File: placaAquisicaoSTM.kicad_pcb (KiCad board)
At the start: 2 copper layers, 55 parts, among them IC1 STM32H523CET6, J1 Conn_01x05, J2 Conn_02x06_Counter_Clockwise, SW1 SW_Push, SW2 SW_SPDT, U1 AMS1117-3.3, U10 PC817, U11 AMS1117-5.0, U12 SN65HVD230, U2 PC817, U3 PC817, U4 PC817, U5 PC817, U6 PC817, U7 PC817, U8 PC817

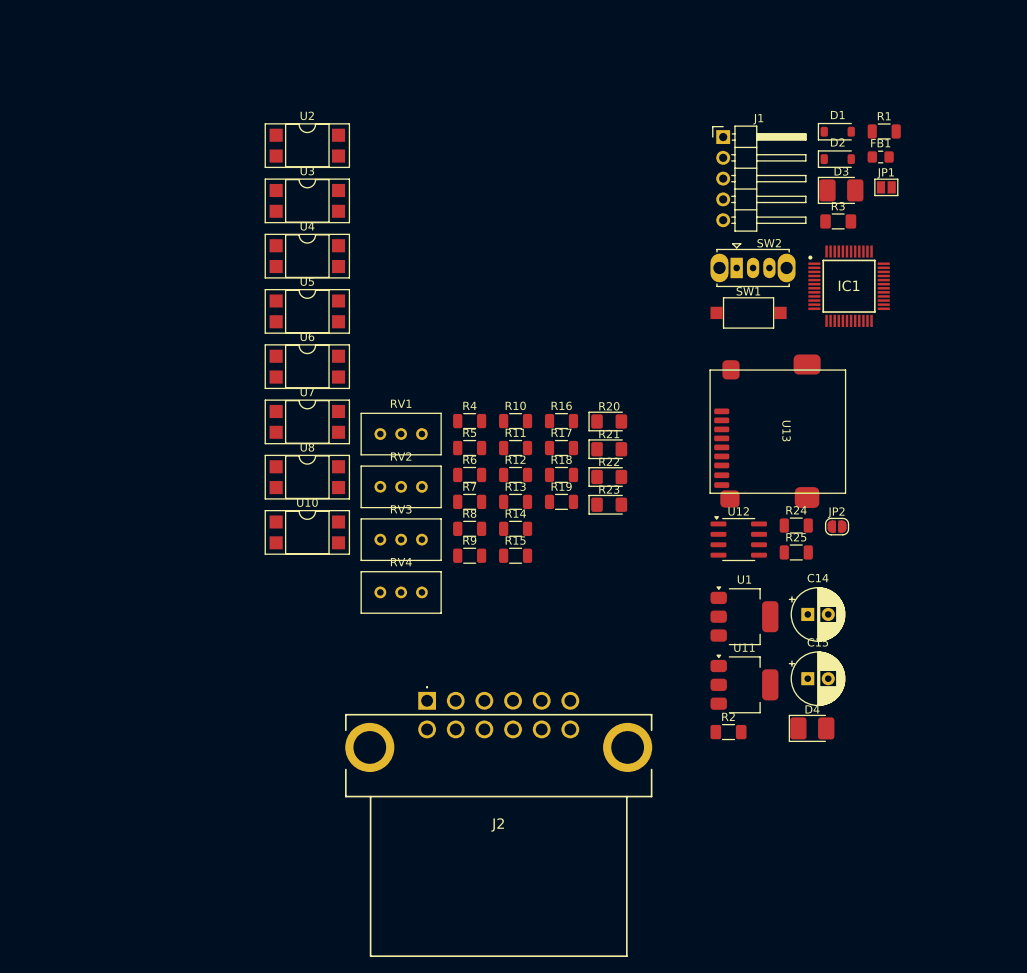
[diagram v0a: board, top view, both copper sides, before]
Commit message: Removi as entradas analógicas, projeto delas estava errado
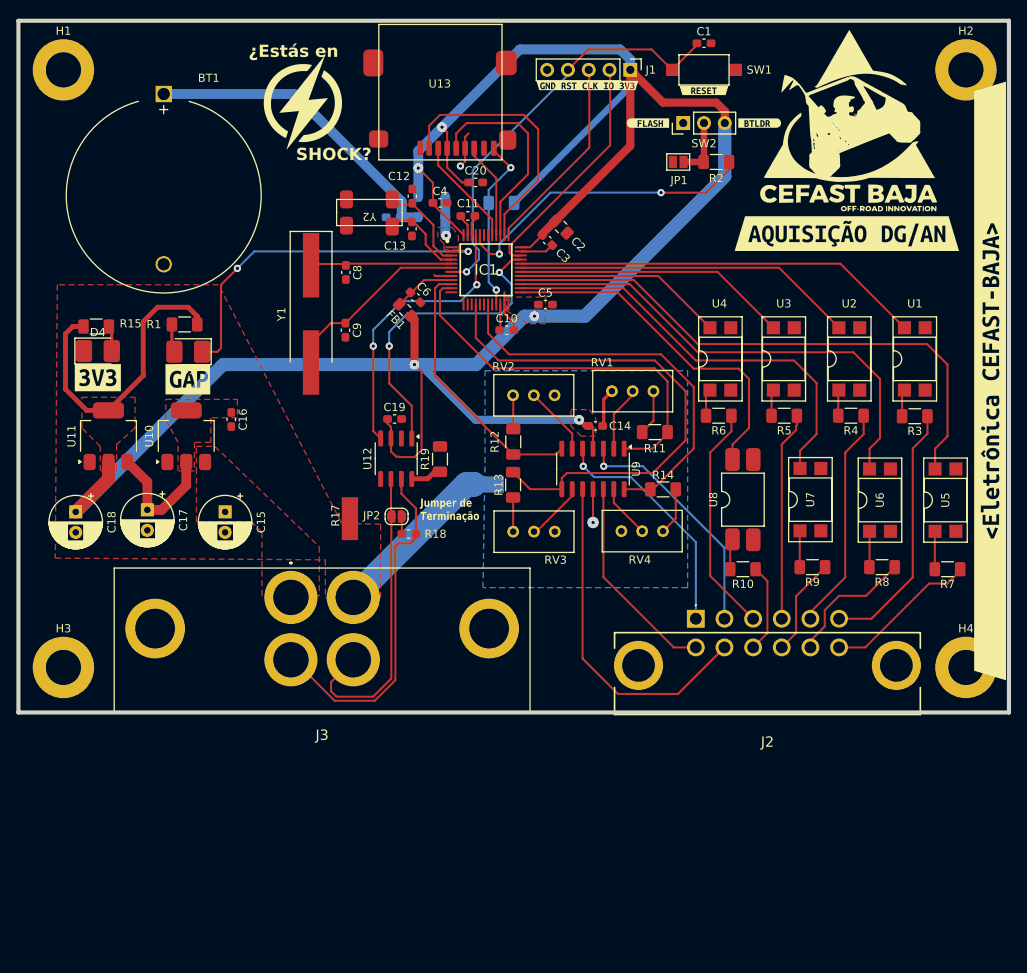
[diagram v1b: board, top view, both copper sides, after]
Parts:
- removed the R10 at (124.2, 93.9)
- removed the R11 at (124.2, 97.2)
- removed the R14 at (124.2, 107.1)
- removed the R19 at (129.8, 103.8)
- removed R25: 120, Resistor_SMD:R_1206_3216Metric
- removed the R6 at (118.6, 100.5)
- removed the R7 at (118.6, 103.8)
- added BT1: Battery_Cell, Battery:BatteryHolder_MYOUNG_BS-07-A1BJ001_CR2032, F.Cu at (81.2, 54.0)
- added C1: 100n, Capacitor_SMD:C_0603_1608Metric_Pad1.08x0.95mm_HandSolder, F.Cu at (147.2, 47.8)
- added C10: 2u2, Capacitor_SMD:C_0603_1608Metric_Pad1.08x0.95mm_HandSolder, F.Cu at (123.2, 82.8)
- added C11: 2u2, Capacitor_SMD:C_0603_1608Metric_Pad1.08x0.95mm_HandSolder, F.Cu at (118.4, 68.8)
- added C12: 22p, Capacitor_SMD:C_0603_1608Metric_Pad1.08x0.95mm_HandSolder, F.Cu at (111.6, 66.4)
- added C13: 22p, Capacitor_SMD:C_0603_1608Metric_Pad1.08x0.95mm_HandSolder, F.Cu at (111.6, 70.4)
- added C14: 1n, Capacitor_SMD:C_0603_1608Metric_Pad1.08x0.95mm_HandSolder, F.Cu at (134.0, 94.5)
- added C15: 22u, Capacitor_THT:CP_Radial_D6.3mm_P2.50mm, F.Cu at (88.8, 105.0)
- added C16: 100n, Capacitor_SMD:C_0603_1608Metric_Pad1.08x0.95mm_HandSolder, F.Cu at (89.5, 93.7)
- added C19: 1n, Capacitor_SMD:C_0603_1608Metric_Pad1.08x0.95mm_HandSolder, F.Cu at (109.5, 93.7)
- added C2: 4u7, Capacitor_SMD:C_0805_2012Metric_Pad1.18x1.45mm_HandSolder, F.Cu at (129.8, 70.2)
- added C20: 1n, Capacitor_SMD:C_0603_1608Metric_Pad1.08x0.95mm_HandSolder, F.Cu at (119.3, 64.8)
- added C3: 100n, Capacitor_SMD:C_0603_1608Metric_Pad1.08x0.95mm_HandSolder, F.Cu at (128.1, 71.8)
- added C4: 100n, Capacitor_SMD:C_0603_1608Metric_Pad1.08x0.95mm_HandSolder, F.Cu at (115.0, 67.2)
- added C5: 100n, Capacitor_SMD:C_0603_1608Metric_Pad1.08x0.95mm_HandSolder, F.Cu at (127.9, 79.7)
- added C6: 10n, Capacitor_SMD:C_0603_1608Metric_Pad1.08x0.95mm_HandSolder, F.Cu at (112.0, 78.8)
- added C7: 100n, Capacitor_SMD:C_0603_1608Metric_Pad1.08x0.95mm_HandSolder, B.Cu at (109.3, 69.0)
- added C8: 22p, Capacitor_SMD:C_0603_1608Metric_Pad1.08x0.95mm_HandSolder, F.Cu at (103.5, 75.8)
- added C9: 22p, Capacitor_SMD:C_0603_1608Metric_Pad1.08x0.95mm_HandSolder, F.Cu at (103.5, 82.8)
- added G***: LOGO, Baja_Library:Raio_Circulo, F.Cu at (98.2, 55.0)
- added G***: LOGO, Baja_Library:LogoBaja, F.Cu at (164.9, 57.2)
- added G***: LOGO, Baja_Library:communism, B.Cu at (172.2, 105.0)
- added G***: LOGO, Baja_Library:Raio_Circulo, B.Cu at (160.3, 102.8)
- added G***: LOGO, Baja_Library:LogoBaja, B.Cu at (165.0, 57.4)
- added H1: MountingHole, MountingHole:MountingHole_4.3mm_M4_DIN965_Pad, F.Cu at (69.0, 51.0)
- added H2: MountingHole, MountingHole:MountingHole_4.3mm_M4_DIN965_Pad, F.Cu at (179.2, 51.0)
- added H3: MountingHole, MountingHole:MountingHole_4.3mm_M4_DIN965_Pad, F.Cu at (69.0, 124.0)
- added H4: MountingHole, MountingHole:MountingHole_4.3mm_M4_DIN965_Pad, F.Cu at (179.2, 124.0)
- added J3: Conn_02x02_Top_Bottom, Baja_Library:MX150L_4P, F.Cu at (96.8, 115.4)
- added R18: 120, Capacitor_SMD:C_0603_1608Metric_Pad1.08x0.95mm_HandSolder, F.Cu at (111.2, 107.7)
- added R20: 10k, Resistor_SMD:R_1206_3216Metric_Pad1.30x1.75mm_HandSolder, B.Cu at (122.5, 67.2)
- added U9: LM324, Package_SO:SOIC-14_3.9x8.7mm_P1.27mm, F.Cu at (133.7, 99.8)
- added Y1: Crystal, Crystal:Crystal_SMD_HC49-SD_HandSoldering, F.Cu at (99.2, 80.8)
- added Y2: Crystal_GND23, Baja_Library:DMX-26S, F.Cu at (106.4, 68.4)
- added kibuzzard-67572A93: G***, kibuzzard-67572A93, F.Cu at (140.4, 57.5)
- added kibuzzard-67572AD3: G***, kibuzzard-67572AD3, F.Cu at (154.1, 57.5)
- added kibuzzard-67572B0D: G***, kibuzzard-67572B0D, F.Cu at (147.2, 53.5)
- added kibuzzard-6758F1AD: G***, kibuzzard-6758F1AD, F.Cu at (84.2, 88.8)
- added kibuzzard-6758F24A: G***, kibuzzard-6758F24A, F.Cu at (73.2, 88.6)
- added kibuzzard-6758F671: G***, kibuzzard-6758F671, F.Cu at (182.2, 89.0)
- added kibuzzard-6758F709: G***, kibuzzard-6758F709, B.Cu at (178.2, 87.8)
- added kibuzzard-6758F727: G***, kibuzzard-6758F727, B.Cu at (182.2, 88.8)
- added kibuzzard-6758FCA4: G***, kibuzzard-6758FCA4, F.Cu at (164.7, 71.0)
- added kibuzzard-6758FCA4: G***, kibuzzard-6758FCA4, B.Cu at (164.6, 71.0)
- added kibuzzard-6758FD86: G***, kibuzzard-6758FD86, F.Cu at (133.0, 52.9)
- D1, D2: moved to B.Cu
- D3, D4: footprint BajaKICAD:LED_1210_HandSoldering -> Baja_Library:LED_1210_HandSoldering
- IC1: footprint BajaKICAD:QFP50P900X900X160-48N -> Baja_Library:QFP50P900X900X160-48N
- J1: footprint Connector_PinHeader_2.54mm:PinHeader_1x05_P2.54mm_Horizontal -> Connector_PinHeader_2.54mm:PinHeader_1x05_P2.54mm_Vertical
- J2: value Conn_02x06_Counter_Clockwise -> Conn_02x06_Top_Bottom; footprint BajaKICAD:MX120G -> Baja_Library:MX120G
- R10: renamed from R18; footprint Resistor_SMD:R_1206_3216Metric -> Resistor_SMD:R_1206_3216Metric_Pad1.30x1.75mm_HandSolder
- R11: renamed from R20; footprint LED_SMD:LED_1206_3216Metric_Pad1.42x1.75mm_HandSolder -> Resistor_SMD:R_1206_3216Metric_Pad1.30x1.75mm_HandSolder
- R12: renamed from R21; footprint LED_SMD:LED_1206_3216Metric_Pad1.42x1.75mm_HandSolder -> Resistor_SMD:R_1206_3216Metric_Pad1.30x1.75mm_HandSolder
- R13: renamed from R22; footprint LED_SMD:LED_1206_3216Metric_Pad1.42x1.75mm_HandSolder -> Resistor_SMD:R_1206_3216Metric_Pad1.30x1.75mm_HandSolder
- R14: renamed from R23; footprint LED_SMD:LED_1206_3216Metric_Pad1.42x1.75mm_HandSolder -> Resistor_SMD:R_1206_3216Metric_Pad1.30x1.75mm_HandSolder
- R16: value 10K -> 0R; footprint Resistor_SMD:R_1206_3216Metric -> Baja_Library:JumperPotencia; moved to B.Cu
- R17: value 10K -> 0R; footprint Resistor_SMD:R_1206_3216Metric -> Baja_Library:JumperPotencia
- R19: renamed from R24; value 10K -> 10k; footprint Resistor_SMD:R_1206_3216Metric -> Resistor_SMD:R_1206_3216Metric_Pad1.30x1.75mm_HandSolder
- R2: renamed from R1; footprint Resistor_SMD:R_1206_3216Metric -> Resistor_SMD:R_1206_3216Metric_Pad1.30x1.75mm_HandSolder
- R3: renamed from R4; footprint Resistor_SMD:R_1206_3216Metric -> Resistor_SMD:R_1206_3216Metric_Pad1.30x1.75mm_HandSolder
- R4: renamed from R8; footprint Resistor_SMD:R_1206_3216Metric -> Resistor_SMD:R_1206_3216Metric_Pad1.30x1.75mm_HandSolder
- R5: renamed from R12; footprint Resistor_SMD:R_1206_3216Metric -> Resistor_SMD:R_1206_3216Metric_Pad1.30x1.75mm_HandSolder
- R6: renamed from R15; footprint Resistor_SMD:R_1206_3216Metric -> Resistor_SMD:R_1206_3216Metric_Pad1.30x1.75mm_HandSolder
- R7: renamed from R5; footprint Resistor_SMD:R_1206_3216Metric -> Resistor_SMD:R_1206_3216Metric_Pad1.30x1.75mm_HandSolder
- R8: renamed from R9; footprint Resistor_SMD:R_1206_3216Metric -> Resistor_SMD:R_1206_3216Metric_Pad1.30x1.75mm_HandSolder
- R9: renamed from R13; footprint Resistor_SMD:R_1206_3216Metric -> Resistor_SMD:R_1206_3216Metric_Pad1.30x1.75mm_HandSolder
- SW2: footprint Button_Switch_THT:SW_Slide_SPDT_Straight_CK_OS102011MS2Q -> Connector_PinHeader_2.54mm:PinHeader_1x03_P2.54mm_Vertical
- U13: footprint BajaKICAD:SD-CARD-GENERIC -> Baja_Library:SD-CARD-GENERIC
- U8: renamed from U7; footprint Package_DIP:DIP-4_W7.62mm_SMDSocket_SmallPads -> Baja_Library:SO-4_HandSoldering
- moved D4 98.7 mm to (73.2, 85.3)
- moved R15 91.8 mm to (73.0, 82.3)
- moved C18 91.7 mm to (70.5, 105.0), turned to -90 degrees
- moved U5 86.1 mm to (176.8, 103.6), turned to 90 degrees
- moved D3 82.2 mm to (84.2, 85.4), turned to 180 degrees
- moved C17 81.7 mm to (79.2, 104.8), turned to -90 degrees
- moved R1 80.8 mm to (83.8, 82.1), turned to 180 degrees
- moved U11 80.8 mm to (74.5, 95.8), turned to 90 degrees
- moved U1 78.6 mm to (173.0, 86.3), turned to 90 degrees
- moved U6 76.0 mm to (168.8, 103.6), turned to 90 degrees
- moved U10 74.7 mm to (84.0, 95.8), turned to 90 degrees
- moved U2 66.5 mm to (165.0, 86.3), turned to 90 degrees
- moved U7 63.6 mm to (160.2, 103.5), turned to 90 degrees
- moved FB1 61.0 mm to (110.8, 80.3), turned to 135 degrees
- moved R7 60.2 mm to (177.0, 112.0), turned to 180 degrees
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- renumbered C14 to C17, C15 to C18, R3 to R1, R2 to R15, U2 to U1, U11 to U10, U1 to U11, U5 to U2, U8 to U3, U10 to U4, U3 to U5, U4 to U6, U6 to U7
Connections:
- net AN3V3 renamed +3.3VA
- net CAN - renamed CAN-
- D1 pad 1: Net-(BT1-+) -> /MicroControlador/VBAT
- D3 pad 1: GND -> /MicroControlador/BD_LED
- IC1 pad 10: unconnected-(IC1-PA0-Pad10) -> AN1
- IC1 pad 11: unconnected-(IC1-PA1-Pad11) -> AN0
- IC1 pad 16: unconnected-(IC1-PA6-Pad16) -> AN2
- IC1 pad 19: unconnected-(IC1-PB1-Pad19) -> AN3
- IC1 pad 2: unconnected-(IC1-PC13-Pad2) -> /MicroControlador/BD_LED
- IC1 pad 21: unconnected-(IC1-PB10-Pad21) -> SD_ON
- IC1 pad 23: GND -> GNDD
- IC1 pad 25: unconnected-(IC1-PB12-Pad25) -> DIG7
- IC1 pad 26: unconnected-(IC1-PB13-Pad26) -> DIG6
- IC1 pad 27: unconnected-(IC1-PB14-Pad27) -> DIG5
- IC1 pad 28: unconnected-(IC1-PB15-Pad28) -> DIG4
- IC1 pad 29: unconnected-(IC1-PA8-Pad29) -> DIG3
- IC1 pad 30: unconnected-(IC1-PA9-Pad30) -> DIG2
- IC1 pad 31: unconnected-(IC1-PA10-Pad31) -> DIG1
- IC1 pad 32: unconnected-(IC1-PA11-Pad32) -> DIG0
- IC1 pad 33: unconnected-(IC1-PA12-Pad33) -> CTX
- IC1 pad 35: GND -> GNDD
- IC1 pad 38: unconnected-(IC1-PA15-Pad38) -> CS_SD
- IC1 pad 39: unconnected-(IC1-PB3-Pad39) -> SCK
- IC1 pad 40: unconnected-(IC1-PB4-Pad40) -> MISO
- IC1 pad 41: unconnected-(IC1-PB5-Pad41) -> MOSI
- IC1 pad 42: unconnected-(IC1-PB6-Pad42) -> TX1
- IC1 pad 43: unconnected-(IC1-PB7-Pad43) -> RX1
- IC1 pad 45: unconnected-(IC1-PB8-Pad45) -> CRX
- IC1 pad 47: GND -> GNDD
- IC1 pad 8: GND -> GNDD
- J1 pad 5: GND -> GNDD
- J2 pad 1: /Portas Analogicas e Digitais/DG_IN_0 -> /Portas Analogicas e Digitais/AN_IN_1
- J2 pad 10: /Portas Analogicas e Digitais/AN_IN_1 -> /Portas Analogicas e Digitais/DG_IN_6
- J2 pad 11: /Portas Analogicas e Digitais/AN_IN_2 -> /Portas Analogicas e Digitais/DG_IN_5
- J2 pad 12: /Portas Analogicas e Digitais/AN_IN_3 -> /Portas Analogicas e Digitais/DG_IN_4
- J2 pad 2: /Portas Analogicas e Digitais/DG_IN_1 -> /Portas Analogicas e Digitais/AN_IN_0
- J2 pad 3: /Portas Analogicas e Digitais/DG_IN_2 -> /Portas Analogicas e Digitais/DG_IN_3
- J2 pad 4: /Portas Analogicas e Digitais/DG_IN_3 -> /Portas Analogicas e Digitais/DG_IN_2
- J2 pad 5: /Portas Analogicas e Digitais/DG_IN_4 -> /Portas Analogicas e Digitais/DG_IN_1
- J2 pad 6: /Portas Analogicas e Digitais/DG_IN_5 -> /Portas Analogicas e Digitais/DG_IN_0
- J2 pad 7: /Portas Analogicas e Digitais/DG_IN_6 -> /Portas Analogicas e Digitais/AN_IN_3
- J2 pad 8: /Portas Analogicas e Digitais/DG_IN_7 -> /Portas Analogicas e Digitais/AN_IN_2
- J2 pad 9: /Portas Analogicas e Digitais/AN_IN_0 -> /Portas Analogicas e Digitais/DG_IN_7
- JP1 pad 1: GND -> GNDD
- R1 pad 1: /MicroControlador/BD_LED -> +3V3
- R11 pad 1: Net-(R20-Pad1) -> AN0
- R12 pad 1: Net-(R21-Pad1) -> AN1
- R13 pad 1: Net-(R22-Pad1) -> AN2
- R14 pad 1: Net-(R23-Pad1) -> AN3
- R16 pad 1: +3V3 -> GND
- R16 pad 2: Net-(R16-Pad2) -> GNDA
- R17 pad 1: +3V3 -> GND
- R17 pad 2: Net-(R17-Pad2) -> GNDD
- R19 pad 2: GND -> GNDD
- RV1 pad 1: GND -> GNDA
- RV2 pad 1: GND -> GNDA
- RV3 pad 1: GND -> GNDA
- RV4 pad 1: GND -> GNDA
- SW1 pad 1: GND -> GNDD
- SW2 pad 1: GND -> GNDD
- U1 pad 2: GND -> GNDD
- U1 pad 3: GND -> GNDD
- U1 pad 4: Net-(R7-Pad2) (its old number) -> DIG0
- U12 pad 2: GND -> GNDD
- U12 pad 7: CAN + -> CAN+
- U13 pad 10: GND -> GNDD
- U13 pad 11: GND -> GNDD
- U13 pad 12: GND -> GNDD
- U13 pad 13: GND -> GNDD
- U13 pad 6: GND -> GNDD
- U13 pad 9: unconnected-(U13-DET-Pad9) -> SD_ON
- U2 pad 2: GND -> GNDD
- U2 pad 3: GND -> GNDD
- U2 pad 4: Net-(R11-Pad2) (its old number) -> DIG1
- U3 pad 2: GND -> GNDD
- U3 pad 3: GND -> GNDD
- U3 pad 4: Net-(R14-Pad2) (its old number) -> DIG2
- U4 pad 2: GND -> GNDD
- U4 pad 3: GND -> GNDD
- U4 pad 4: Net-(R17-Pad2) -> DIG3
- U5 pad 2: GND -> unconnected-(U5-Pad2)
- U5 pad 3: GND -> GNDD
- U5 pad 4: Net-(R6-Pad2) (its old number) -> DIG4
- U6 pad 2: GND -> GNDD
- U6 pad 3: GND -> GNDD
- U6 pad 4: Net-(R10-Pad2) (its old number) -> DIG5
- U7 pad 2: GND -> GNDD
- U7 pad 3: GND -> GNDD
- U7 pad 4: Net-(R16-Pad2) -> DIG6
- U8 pad 2: GND -> GNDD
- U8 pad 3: GND -> GNDD
- U8 pad 4: Net-(R19-Pad2) -> DIG7
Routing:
- net +3V3: track 0.00 -> 347.0 mm, vias 0 -> 5
- net DIG4: track 0.00 -> 69.8 mm
- net AN2: track 0.00 -> 63.6 mm
- net DIG5: track 0.00 -> 60.2 mm
- net DIG6: track 0.00 -> 52.2 mm
- net /MicroControlador/NRST: track 0.00 -> 51.5 mm, vias 0 -> 1
- net DIG0: track 0.00 -> 50.1 mm
- net AN3: track 0.00 -> 49.4 mm
- net AN0: track 0.00 -> 47.7 mm
- net /MicroControlador/BD_LED: track 0.00 -> 44.2 mm, vias 0 -> 2
- net CAN+: track 0.00 -> 44.1 mm
- net DIG7: track 0.00 -> 44.0 mm
- net /Portas Analogicas e Digitais/AN_IN_2: track 0.00 -> 42.2 mm
- net DIG1: track 0.00 -> 41.9 mm
- net Net-(BT1-+): track 0.00 -> 38.5 mm
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- added copper zone on F.Cu, net +12V
- added copper zone on F.Cu, net +3V3
- added copper zone on F.Cu, net +5V
- added copper zone on F.Cu, net /MicroControlador/VBAT
- added copper zone on F.Cu, net GND
- added copper zone on B.Cu, net GNDA
- added copper zone on B.Cu, net GNDD
- added copper zone on F.Cu, net GNDD
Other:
- board outline added: 121 x 84.5 mm
- board text added: "(Are you em shoqui?)"
- board text added: "FIM DA 6x1"
- board text added: "I LOVE PWT"
- board text added: "Jumper de Terminação"
- board text added: "SHOCK?"
- board text added: "¿Estás en"

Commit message: Alterei para ter 3 portas analogicas, adaptei o circuito do RPM para ter um jumper que permite usar como entrada digital
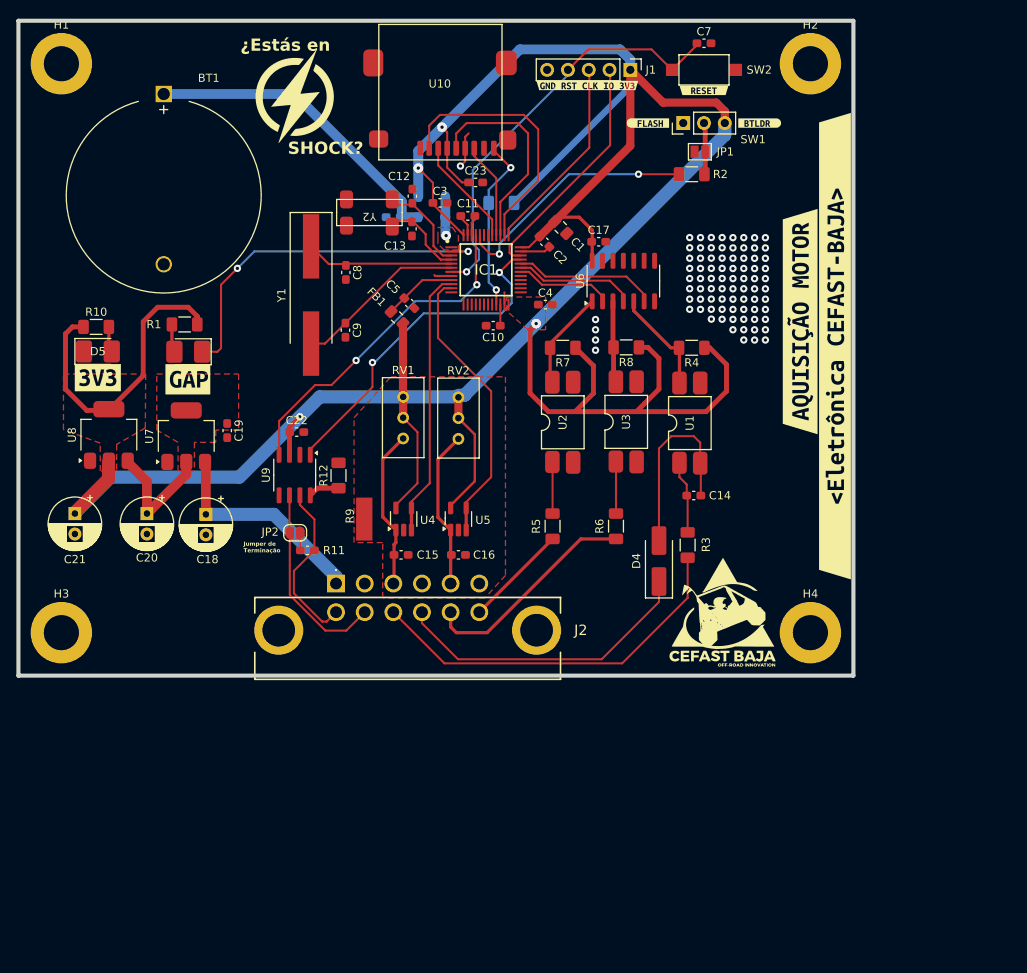
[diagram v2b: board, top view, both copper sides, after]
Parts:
- removed the G*** at (172.2, 105.0)
- removed J3: Conn_02x02_Top_Bottom, Baja_Library:MX150L_4P
- removed the R11 at (141.2, 95.2)
- removed the R12 at (124.0, 96.4)
- removed the R13 at (123.9, 101.7)
- removed R14, R15: 1k, Resistor_SMD:R_1206_3216Metric_Pad1.30x1.75mm_HandSolder
- removed R16, R17: 0R, Baja_Library:JumperPotencia
- removed the R5 at (157.1, 93.2)
- removed the R6 at (149.1, 93.2)
- removed RV3, RV4: 10k_trim, Potentiometer_THT:Potentiometer_Bourns_3296W_Vertical
- removed the U10 at (84.0, 95.8)
- removed U11: AMS1117-3.3, Package_TO_SOT_SMD:SOT-223-3_TabPin2
- removed the U3 at (157.0, 86.3)
- removed the U9 at (133.7, 99.8)
- removed kibuzzard-6758F671: G***, kibuzzard-6758F671
- removed kibuzzard-6758FCA4 (x2): G***, kibuzzard-6758FCA4
- added C19: 100n, Capacitor_SMD:C_0603_1608Metric_Pad1.08x0.95mm_HandSolder, F.Cu at (89.0, 95.1)
- added C20: 22u, Capacitor_THT:CP_Radial_D6.3mm_P2.50mm, F.Cu at (79.2, 105.2)
- added C21: 22u, Capacitor_THT:CP_Radial_D6.3mm_P2.50mm, F.Cu at (70.4, 105.2)
- added D5: LED, Baja_Library:LED_1210_HandSoldering, F.Cu at (73.2, 85.4)
- added R3: 680, Resistor_SMD:R_1206_3216Metric_Pad1.30x1.75mm_HandSolder, F.Cu at (145.2, 109.0)
- added R4: 10k, Resistor_SMD:R_1206_3216Metric_Pad1.30x1.75mm_HandSolder, F.Cu at (145.8, 85.0)
- added U1: PC817, Baja_Library:SO-4_HandSoldering, F.Cu at (145.5, 94.2)
- added kibuzzard-67891694: G***, kibuzzard-67891694, F.Cu at (159.0, 81.8)
- added kibuzzard-67897D6F: G***, kibuzzard-67897D6F, F.Cu at (163.2, 84.8)
- C14: value 1n -> 10u
- C15, C17: value 22u -> 1n; footprint Capacitor_THT:CP_Radial_D6.3mm_P2.50mm -> Capacitor_SMD:C_0603_1608Metric_Pad1.08x0.95mm_HandSolder
- C16: value 100n -> 1n
- D4: value LED -> D; footprint Baja_Library:LED_1210_HandSoldering -> Diode_SMD:D_SMA_Handsoldering
- R10: value 680 -> 1k
- R7, R8: value 680 -> 10k
- R9: value 680 -> 0R; footprint Resistor_SMD:R_1206_3216Metric_Pad1.30x1.75mm_HandSolder -> Baja_Library:JumperPotencia
- U2: renamed from U1; footprint Package_DIP:DIP-4_W7.62mm_SMDSocket_SmallPads -> Baja_Library:SO-4_HandSoldering
- U3: renamed from U2; footprint Package_DIP:DIP-4_W7.62mm_SMDSocket_SmallPads -> Baja_Library:SO-4_HandSoldering
- U4, U5: value PC817 -> LMV321; footprint Package_DIP:DIP-4_W7.62mm_SMDSocket_SmallPads -> Package_TO_SOT_SMD:SOT-23-5_HandSoldering
- U6: value PC817 -> 74HC14; footprint Package_DIP:DIP-4_W7.62mm_SMDSocket_SmallPads -> Package_SO:SOIC-14_3.9x8.7mm_P1.27mm
- U7: value PC817 -> AMS1117-5.0; footprint Package_DIP:DIP-4_W7.62mm_SMDSocket_SmallPads -> Package_TO_SOT_SMD:SOT-223-3_TabPin2
- U8: value PC817 -> AMS1117-3.3; footprint Baja_Library:SO-4_HandSoldering -> Package_TO_SOT_SMD:SOT-223-3_TabPin2
- moved R10 84.4 mm to (73.0, 82.4), turned to 0 degrees
- moved U8 77.9 mm to (74.5, 95.6)
- moved U7 76.6 mm to (84.0, 95.8)
- moved D4 73.2 mm to (141.8, 111.0), turned to 90 degrees
- moved C17 64.1 mm to (134.4, 72.0), turned to 0 degrees
- moved G*** 62.0 mm to (149.5, 117.2)
- moved U5 59.5 mm to (117.2, 105.9)
- moved R9 55.1 mm to (105.8, 105.8), turned to 90 degrees
- moved R7 54.2 mm to (130.0, 85.0)
- moved R5 46.2 mm to (128.8, 106.8), turned to 90 degrees
- moved J2 44.2 mm to (102.3, 113.8)
- moved U2 43.7 mm to (130.0, 94.0)
- moved U4 43.4 mm to (110.6, 105.9)
- moved U6 41.2 mm to (137.4, 76.8)
- moved R8 41.2 mm to (137.8, 84.9)
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- renumbered C2 to C1, C3 to C2, C19 to C22, C20 to C23, C4 to C3, C5 to C4, C6 to C5, C7 to C6, C1 to C7, R18 to R11, R19 to R12, R20 to R13, R3 to R5, R4 to R6, SW2 to SW1, SW1 to SW2, U13 to U10, U12 to U9
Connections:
- BT1 pad 2: GNDD -> GND
- C1 pad 2: GNDD -> GND
- C10 pad 2: GNDD -> GND
- C11 pad 2: GNDD -> GND
- C12 pad 2: GNDD -> GND
- C13 pad 2: GNDD -> GND
- C14 pad 1: +3V3 -> Net-(C14-Pad1)
- C14 pad 2: GNDA -> Net-(D4-A)
- C15 pad 1: +12V -> NTC_P1
- C15 pad 2: GND -> NTC_N1
- C16 pad 1: +5V -> NTC_P2
- C16 pad 2: GND -> NTC_N1
- C17 pad 1: +5V -> +3V3
- C18 pad 1: +3V3 -> +12V
- C2 pad 2: GNDD -> GND
- C22 pad 2: GNDD -> GND
- C23 pad 2: GNDD -> GND
- C3 pad 2: GNDD -> GND
- C4 pad 2: GNDD -> GND
- C5 pad 2: GNDD -> GND
- C6 pad 2: GNDD -> GND
- C7 pad 2: GNDD -> GND
- C8 pad 2: GNDD -> GND
- C9 pad 2: GNDD -> GND
- D4 pad 1: GND -> MTMT
- IC1 pad 10: AN1 -> NTC_AN_1
- IC1 pad 11: AN0 -> NTC_AN_2
- IC1 pad 16: AN2 -> unconnected-(IC1-PA6-Pad16)
- IC1 pad 19: AN3 -> unconnected-(IC1-PB1-Pad19)
- IC1 pad 23: GNDD -> GND
- IC1 pad 25: DIG7 -> unconnected-(IC1-PB12-Pad25)
- IC1 pad 26: DIG6 -> unconnected-(IC1-PB13-Pad26)
- IC1 pad 27: DIG5 -> unconnected-(IC1-PB14-Pad27)
- IC1 pad 28: DIG4 -> unconnected-(IC1-PB15-Pad28)
- IC1 pad 29: DIG3 -> unconnected-(IC1-PA8-Pad29)
- IC1 pad 35: GNDD -> GND
- IC1 pad 47: GNDD -> GND
- IC1 pad 8: GNDD -> GND
- J1 pad 5: GNDD -> GND
- J2 pad 1: /Portas Analogicas e Digitais/AN_IN_1 -> +12V
- J2 pad 10: /Portas Analogicas e Digitais/DG_IN_6 -> MTMT
- J2 pad 11: /Portas Analogicas e Digitais/DG_IN_5 -> OPTO_IN_1
- J2 pad 12: /Portas Analogicas e Digitais/DG_IN_4 -> OPTO_IN_0
- J2 pad 2: /Portas Analogicas e Digitais/AN_IN_0 -> GND
- J2 pad 3: /Portas Analogicas e Digitais/DG_IN_3 -> NTC_P1
- J2 pad 4: /Portas Analogicas e Digitais/DG_IN_2 -> NTC_N1
- J2 pad 5: /Portas Analogicas e Digitais/DG_IN_1 -> NTC_P2
- J2 pad 6: /Portas Analogicas e Digitais/DG_IN_0 -> NTC_N1
- J2 pad 7: /Portas Analogicas e Digitais/AN_IN_3 -> CAN+
- J2 pad 8: /Portas Analogicas e Digitais/AN_IN_2 -> CAN-
- J2 pad 9: /Portas Analogicas e Digitais/DG_IN_7 -> CHASSI
- JP1 pad 1: GNDD -> GND
- R10 pad 1: /Portas Analogicas e Digitais/DG_IN_7 -> +3V3
- R10 pad 2: Net-(R10-Pad2) -> Net-(D5-A)
- R12 pad 2: GNDD -> GND
- R5 pad 1: /Portas Analogicas e Digitais/DG_IN_0 -> OPTO_IN_0
- R6 pad 1: /Portas Analogicas e Digitais/DG_IN_1 -> OPTO_IN_1
- R7 pad 1: /Portas Analogicas e Digitais/DG_IN_4 -> +3V3
- R7 pad 2: Net-(R7-Pad2) -> OPTO_0
- R8 pad 1: /Portas Analogicas e Digitais/DG_IN_5 -> +3V3
- R8 pad 2: Net-(R8-Pad2) -> OPTO_1
- R9 pad 1: /Portas Analogicas e Digitais/DG_IN_6 -> GND
- R9 pad 2: Net-(R9-Pad2) -> NTC_N1
- RV1 pad 1: GNDA -> +3V3
- RV1 pad 2: Net-(U9A--) -> +3V3
- RV1 pad 3: Net-(R11-Pad2) -> NTC_P1
- RV2 pad 1: GNDA -> +3V3
- RV2 pad 2: Net-(U9B--) -> +3V3
- RV2 pad 3: Net-(R12-Pad2) -> NTC_P2
- SW1 pad 1: GNDD -> GND
- SW2 pad 1: GNDD -> GND
- U10 pad 10: GNDD -> GND
- U10 pad 11: GNDD -> GND
- U10 pad 12: GNDD -> GND
- U10 pad 13: GNDD -> GND
- U10 pad 6: GNDD -> GND
- U2 pad 2: GNDD -> GND
- U2 pad 3: GNDD -> GND
- U2 pad 4: DIG0 -> OPTO_0
- U3 pad 2: GNDD -> GND
- U3 pad 3: GNDD -> GND
- U3 pad 4: DIG1 -> OPTO_1
- U4 pad 1: Net-(R6-Pad2) (its old number) -> NTC_P1
- U4 pad 2: GNDD -> NTC_N1
- U4 pad 3: GNDD -> NTC_AN_1
- U4 pad 4: DIG3 -> NTC_AN_1
- U5 pad 1: Net-(R7-Pad2) -> NTC_P2
- U5 pad 2: unconnected-(U5-Pad2) -> NTC_N1
- U5 pad 3: GNDD -> NTC_AN_2
- U5 pad 4: DIG4 -> NTC_AN_2
- U6 pad 1: Net-(R8-Pad2) -> OPTO_0
- U6 pad 2: GNDD -> DIG2
- U6 pad 3: GNDD -> OPTO_1
- U6 pad 4: DIG5 -> DIG1
- U7 pad 1: Net-(R9-Pad2) -> GND
- U7 pad 2: GNDD -> +5V
- U7 pad 3: GNDD -> +12V
- U8 pad 1: Net-(R10-Pad2) -> GND
- U8 pad 2: GNDD -> +3V3
- U8 pad 3: GNDD -> +5V
- U9 pad 2: GNDD -> GND
- Y2 pad 2: GNDD -> GND
- Y2 pad 3: GNDD -> GND
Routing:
- net DIG4: track 69.8 -> 0.00 mm
- net AN2: track 63.6 -> 0.00 mm
- net DIG5: track 60.2 -> 0.00 mm
- net DIG6: track 52.2 -> 0.00 mm
- net AN3: track 49.4 -> 0.00 mm
- net AN0: track 47.7 -> 0.00 mm
- net CHASSI: track 0.00 -> 46.8 mm
- net DIG7: track 44.0 -> 0.00 mm
- net /Portas Analogicas e Digitais/AN_IN_2: track 42.2 -> 0.00 mm
- net MTMT: track 0.00 -> 37.5 mm
- net +3V3: track 347.0 -> 384.2 mm, vias 5 -> 4
- net NTC_AN_2: track 0.00 -> 34.7 mm
- net NTC_AN_1: track 0.00 -> 32.7 mm
- net AN1: track 32.7 -> 0.00 mm
- net DIG0: track 50.1 -> 17.5 mm
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- added copper zone on B.Cu, net GND
- added copper zone on F.Cu, net NTC_N1
- removed copper zone on F.Cu, net +12V
- removed copper zone on B.Cu, net GNDA
- removed copper zone on B.Cu, net GNDD
- removed copper zone on F.Cu, net GNDD
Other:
- board size 121 x 84.5 mm -> 102 x 80 mm
- board text removed: "(Are you em shoqui?)"
- board text removed: "FIM DA 6x1"
